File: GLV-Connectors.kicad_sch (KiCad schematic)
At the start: 3 parts, among them J1 1053091104, J2 DTF13-4P-G003, J4 DTF13-4P-G003

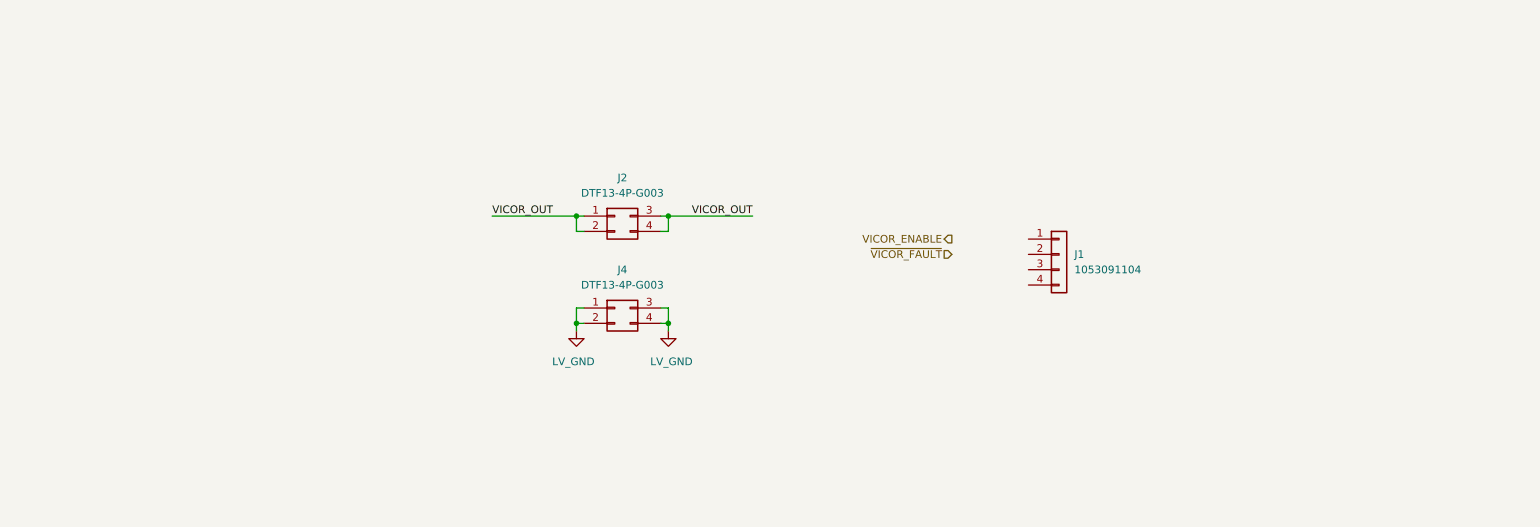
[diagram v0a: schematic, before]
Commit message: Finished up draft 1 of schematic
Need to look everything over and do a quick layout
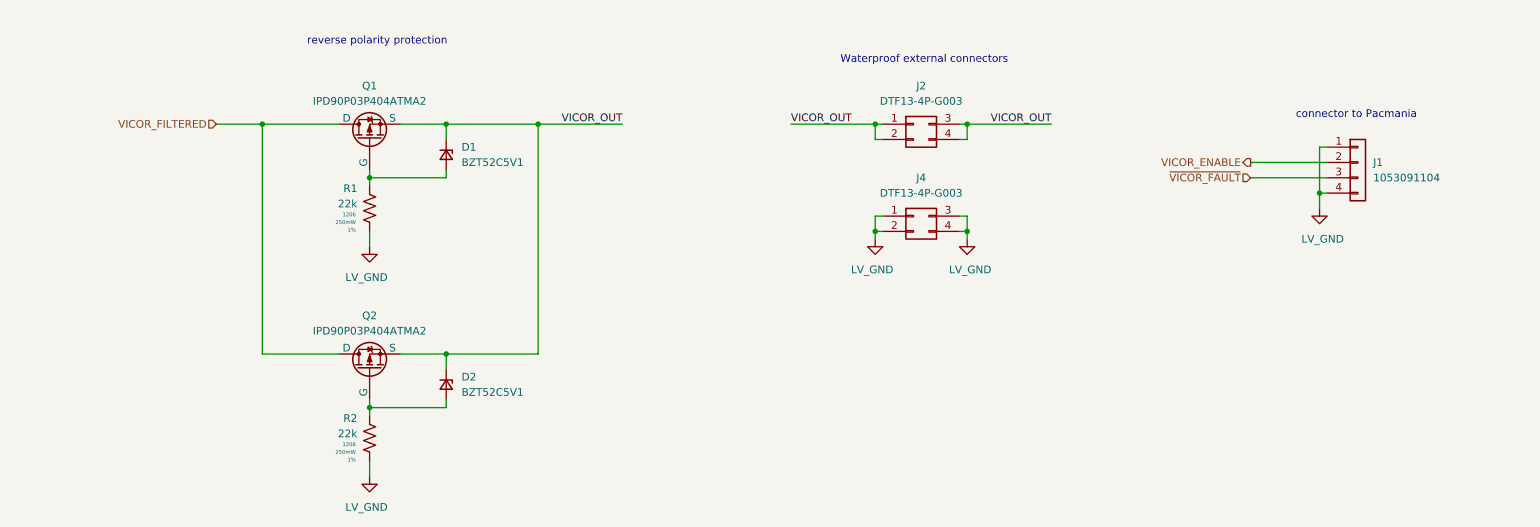
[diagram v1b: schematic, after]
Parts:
- added D1, D2: BZT52C5V1, Diode_SMD:D_SOD-123F, symbol Device:D_Zener_Small
- added Q1, Q2: IPD90P03P404ATMA2, AERO_Transistors:IPD90P03P404ATMA2, symbol AERO_Transistors:IPD90P03P404ATMA2
- added R1, R2: 22k, Resistor_SMD:R_1206_3216Metric_Pad1.30x1.75mm_HandSolder, symbol AERO_Resistors:R_1206
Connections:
- net LV_GND: now also J1.1 (Pin_1), J1.4 (Pin_4), R1.1, R2.1
- net VICOR_ENABLE: now also J1.2 (Pin_2)
- net VICOR_OUT: now also D1.1 (K), D2.1 (K), Q1.3 (S), Q2.3 (S)
- net ~{VICOR_FAULT}: now also J1.3 (Pin_3)
- new net: D2.2 (A), Q2.2 (G), R2.2
- new net: D1.2 (A), Q1.2 (G), R1.2
- new net VICOR_FILTERED: Q1.1 (D), Q2.1 (D)
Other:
- note added: "Waterproof external connectors"
- note added: "connector to Pacmania"
- note added: "reverse polarity protection"
- moved on the sheet: J1, J2, J4

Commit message: Started layout
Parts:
- added C8: 100u, Capacitor_THT:C_Radial_D12.5mm_H25.0mm_P5.00mm, symbol Device:C_Small
- renumbered J2 to J1, J4 to J2, J1 to J3
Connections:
- net LV_GND: now also C8.2; no longer J3.1 (Pin_1)
- net VICOR_FILTERED: now also C8.1
- new net TSMS12V: J3.1 (Pin_1)

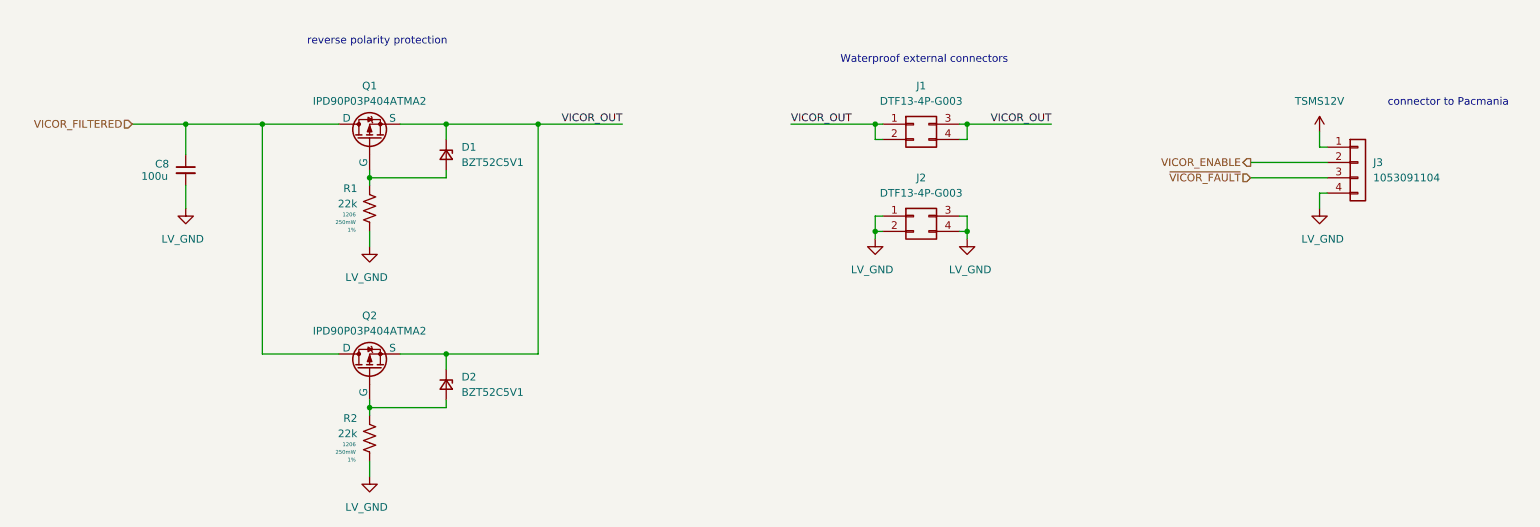
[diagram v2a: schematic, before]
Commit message: Routing and clearance changes. Added board cutouts and mounting holes
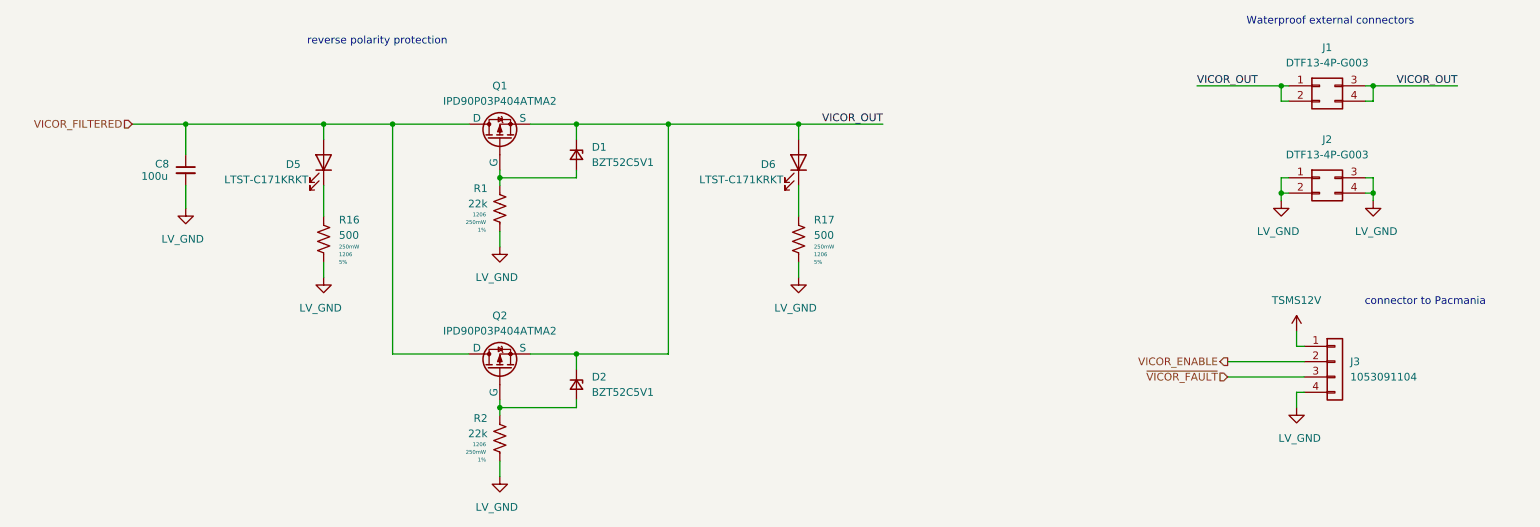
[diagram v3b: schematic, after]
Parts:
- added D5, D6: LTST-C171KRKT, LED_SMD:LED_0805_2012Metric, symbol Device:LED
- added R16, R17: 500, Resistor_SMD:R_1206_3216Metric_Pad1.30x1.75mm_HandSolder, symbol AERO_Resistors:R_1206
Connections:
- net LV_GND: now also R16.1, R17.1
- net VICOR_FILTERED: now also D5.2 (A)
- net VICOR_OUT: now also D6.2 (A)
- new net: D6.1 (K), R17.2
- new net: D5.1 (K), R16.2
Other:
- moved on the sheet: D1, D2, J1, J2, J3, Q1, Q2, R1, R2
